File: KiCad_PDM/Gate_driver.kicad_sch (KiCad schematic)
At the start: 26 parts, among them U10 INA180A3IDBVR, U6 2N7002, U7 NSG2000, U8 OSP80N03T, U9 2N7002

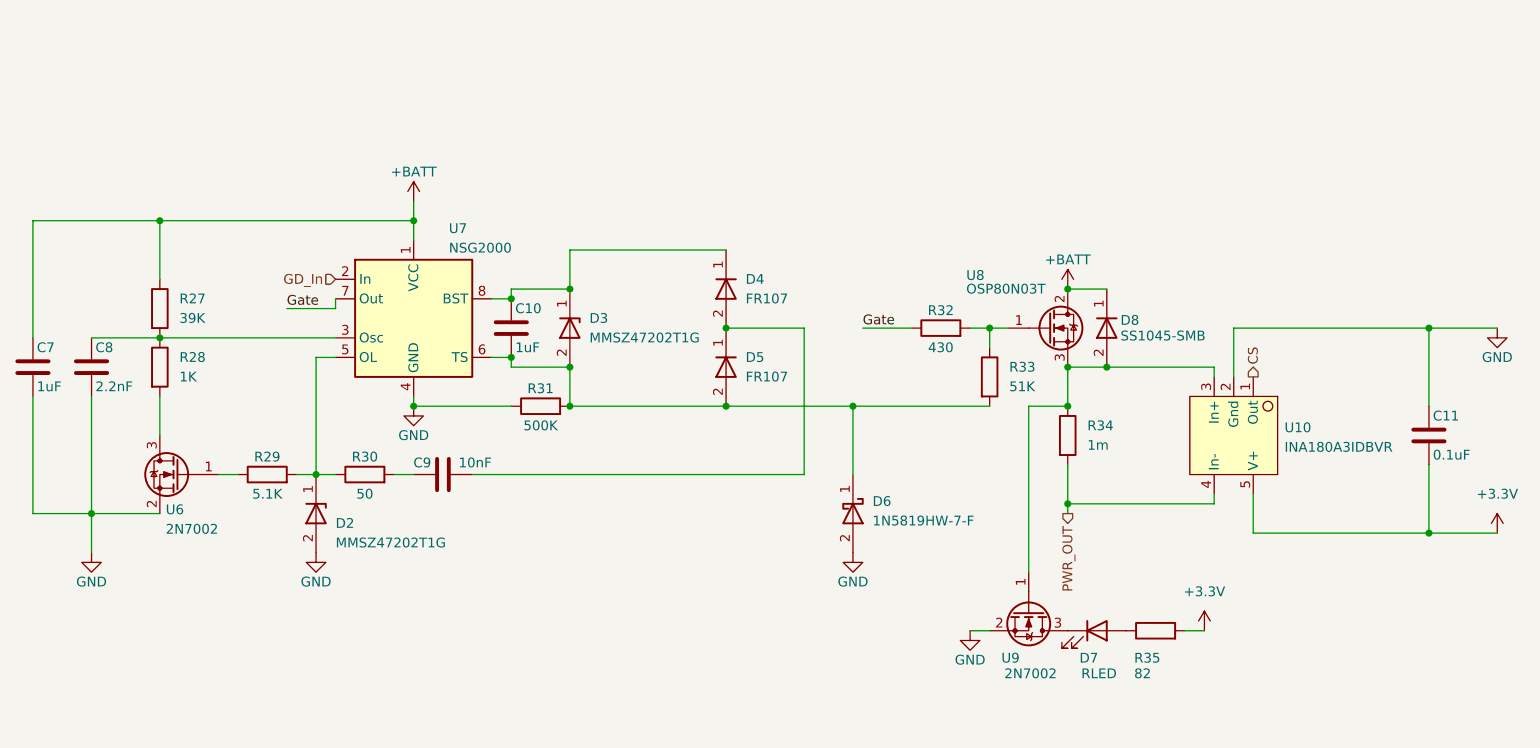
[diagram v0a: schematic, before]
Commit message: Added TS/Souce connections, fixed flyback diode connections, fixed current sense kelvin connections
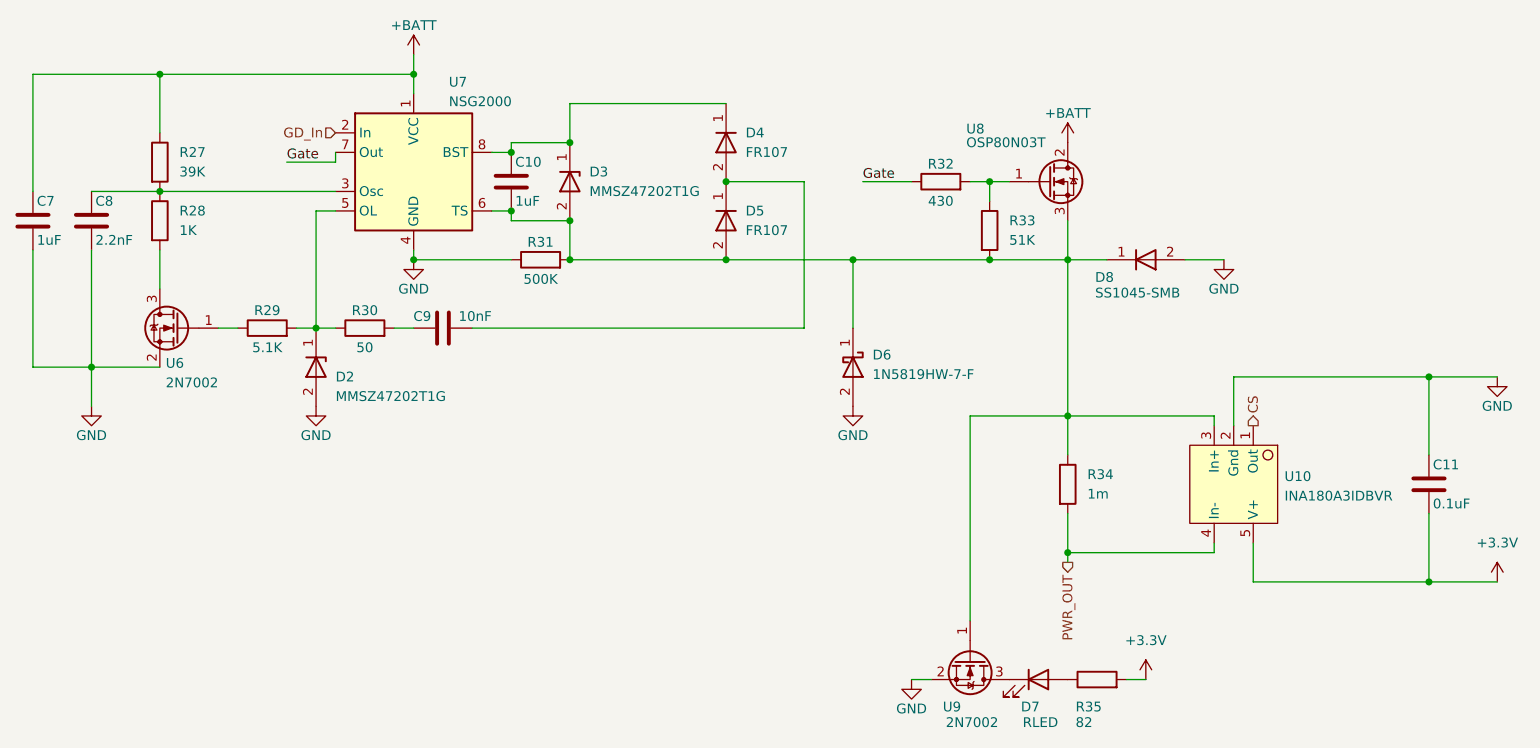
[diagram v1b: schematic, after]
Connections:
- net +BATT: no longer D8.1
- net GND: now also D8.2
- net at R34.1, U10.3 (In+), U8.3 (Source)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: now also C10.2, D3.2, D5.2, D6.1 (K), D8.1, R31.2, R33.2, U7.6 (TS); no longer D8.2
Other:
- moved on the sheet: C10, C11, C7, C8, C9, D2, D3, D4, D5, D6, D7, D8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
